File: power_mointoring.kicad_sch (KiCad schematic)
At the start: 25 parts, among them J10 Servo pwr, J11 Vin, J13 VCC, J7 VCC, J8 Servo pwr, J9 BATT in, SW5 POWER, U3 3V3 REG, U4 DS2438Z+, U5 DS2438Z+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

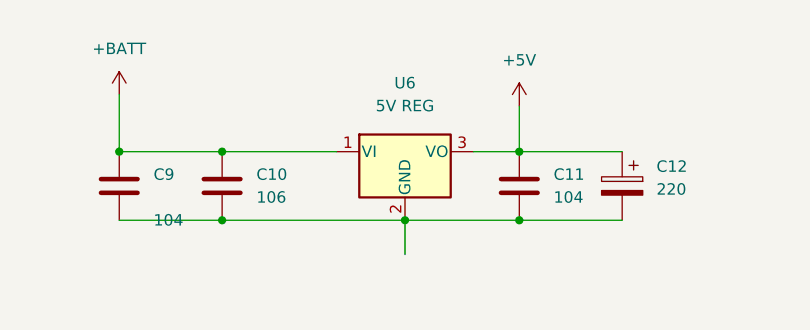
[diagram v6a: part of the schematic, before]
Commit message: Very minor tweaks for board version 3.
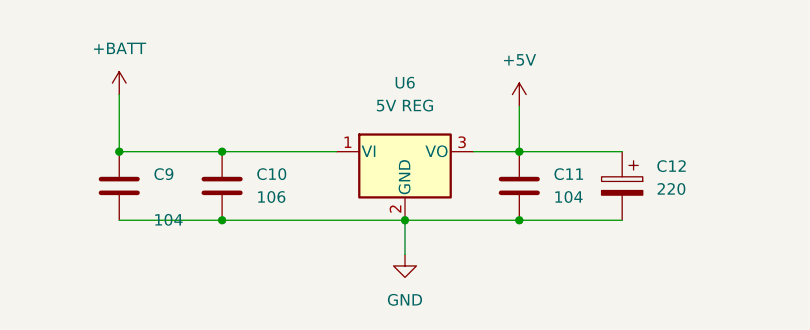
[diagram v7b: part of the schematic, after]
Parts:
- R25: footprint Resistor_SMD:R_1206_3216Metric_Pad1.30x1.75mm_HandSolder -> Resistor_SMD:R_1812_4532Metric_Pad1.30x3.40mm_HandSolder
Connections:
- net GND: now also C10.2, C11.2, C12.2, C9.2, U6.2 (GND)
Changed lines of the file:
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@@
       (effects (font (size 1.27 1.27)) (justify right))
     )
-    (property "Footprint" "Resistor_SMD:R_1206_3216Metric_Pad1.30x1.75mm_HandSolder" (id 2) (at 143.51 94.488 90)
+    (property "Footprint" "Resistor_SMD:R_1812_4532Metric_Pad1.30x3.40mm_HandSolder" (id 2) (at 143.51 94.488 90)
       (effects (font (size 1.27 1.27)) hide)
     )
@@
       (effects (font (size 1.27 1.27)) hide)
     )
+    (pin "1")
+  )
+  (symbol (lib_id "power:GND") (at 97.79 191.77 0) (unit 1)
+    (in_bom yes) (on_board yes) (fields_autoplaced)
+    (property "Reference" "#PWR0184" (id 0) (at 97.79 198.12 0)
+      (effects (font (size 1.27 1.27)) hide)
+    )
+    (property "Value" "GND" (id 1) (at 97.79 196.85 0))
+    (property "Footprint" "" (id 2) (at 97.79 191.77 0)
+      (effects (font (size 1.27 1.27)) hide)
+    )
+    (property "Datasheet" "" (id 3) (at 97.79 191.77 0)
+      (effects (font (size 1.27 1.27)) hide)
+    )

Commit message: Upgrade to version 7, started adding new WROOM-S3
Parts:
- J11, J9: footprint Connector_PinHeader_2.54mm:Connector_Battery_SolderPads -> Connector_JST:JST_VH_B2P-VH-B_1x02_P3.96mm_Vertical
